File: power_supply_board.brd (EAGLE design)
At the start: 100 x 65 mm, 30 parts, among them J6 1744426-2

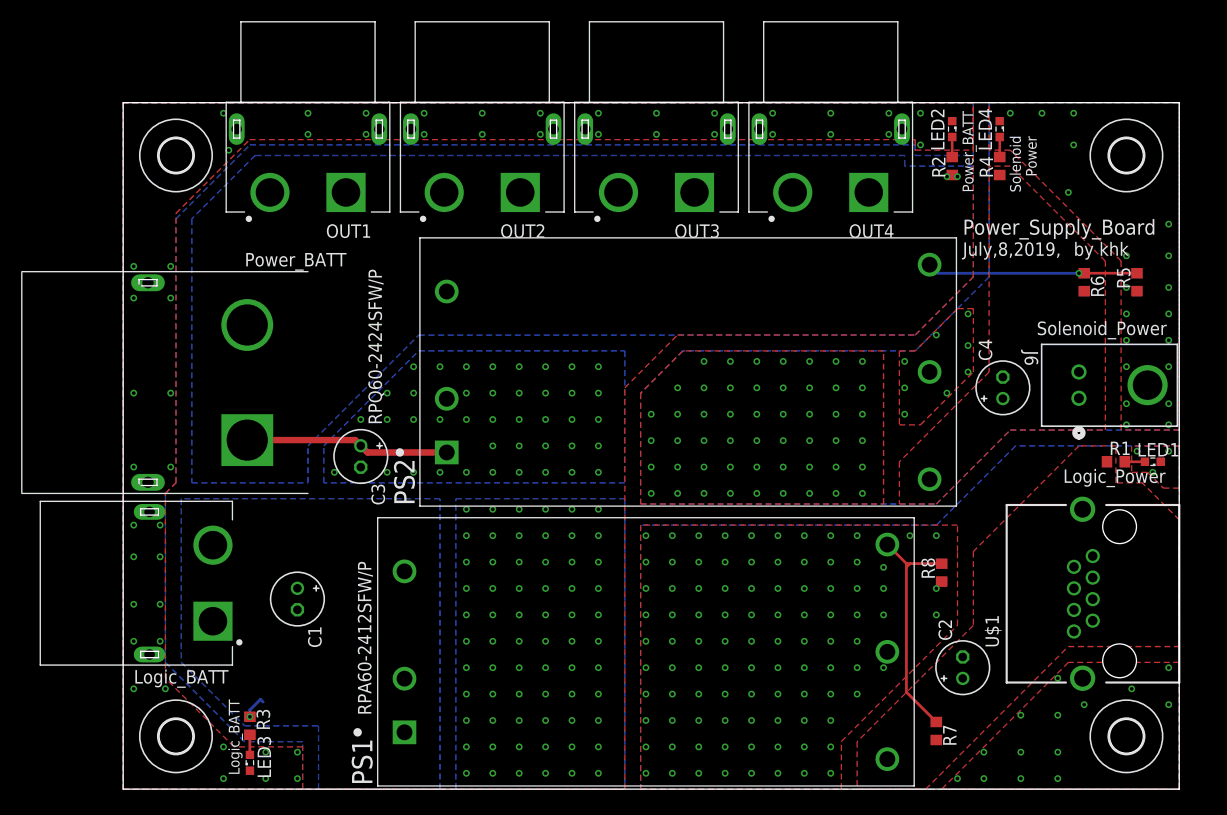
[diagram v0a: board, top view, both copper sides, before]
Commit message: xt及びコンバータのthermalを外した
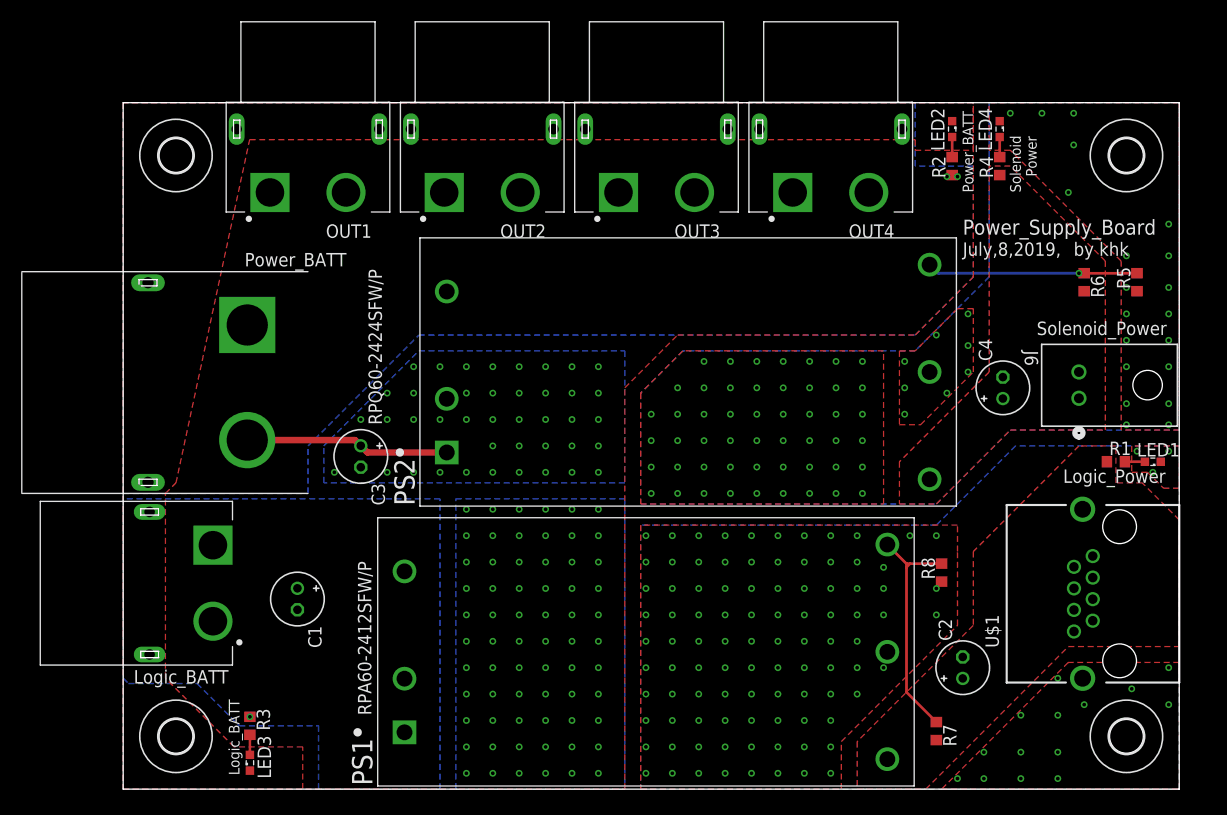
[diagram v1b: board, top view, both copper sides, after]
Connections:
- net DGND: now also OUT1.1, OUT2.1, OUT3.1, OUT4.1, POWER1.2; no longer OUT1.2, OUT2.2, OUT3.2, OUT4.2, POWER1.1
- net LOGIC_BATT: now also POWER1.1; no longer POWER1.2
- net POWER_BATT: now also OUT1.2, OUT2.2, OUT3.2, OUT4.2; no longer OUT1.1, OUT2.1, OUT3.1, OUT4.1
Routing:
- net LOGIC_BATT: track 2.42 -> 0.15 mm

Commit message: ガーバーファイルを追加
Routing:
- net POWER_BATT: track 20.5 -> 9.53 mm
- net DGND: track 0.00 -> 11.0 mm, vias 107 -> 98
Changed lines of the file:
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@@
 <setting verticaltext="up"/>
 </settings>
-<grid distance="0.5" unitdist="mm" unit="mm" style="lines" multiple="1" display="yes" altdistance="0.1" altunitdist="mm" altunit="mm"/>
+<grid distance="4" unitdist="mil" unit="mil" style="lines" multiple="1" display="yes" altdistance="2" altunitdist="mil" altunit="mil"/>
 <layers>
 <layer number="1" name="Top" color="4" fill="1" visible="yes" active="yes"/>
@@
 <text x="79.5" y="50.5" size="1.27" layer="25">July,8,2019,</text>
 <text x="90" y="50.5" size="1.27" layer="25">by khk</text>
-<rectangle x1="11.5" y1="49" x2="66" y2="54" layer="30"/>
-<rectangle x1="11.5" y1="54" x2="16.5" y2="59" layer="30"/>
-<rectangle x1="28" y1="54" x2="33" y2="59" layer="30"/>
-<rectangle x1="44.5" y1="54" x2="49.5" y2="59" layer="30"/>
-<rectangle x1="61" y1="54" x2="66" y2="59" layer="30"/>
-<rectangle x1="8.5" y1="40.5" x2="17" y2="47" layer="30"/>
-<rectangle x1="11.5" y1="47" x2="17" y2="49" layer="30"/>
+<rectangle x1="18.5" y1="49" x2="73" y2="54" layer="30"/>
+<rectangle x1="18.5" y1="54" x2="23.5" y2="59" layer="30"/>
+<rectangle x1="35" y1="54" x2="40" y2="59" layer="30"/>
+<rectangle x1="51.5" y1="54" x2="56.5" y2="59" layer="30"/>
+<rectangle x1="68" y1="54" x2="73" y2="59" layer="30"/>
+<rectangle x1="8" y1="30" x2="16.5" y2="36.5" layer="30"/>
+<rectangle x1="18.5" y1="35" x2="24" y2="49" layer="30"/>
+<rectangle x1="13" y1="32" x2="23" y2="38.5" layer="30" rot="R30"/>
 </plain>
 <attributes>
@@
 <vertex x="0" y="65"/>
 </polygon>
-<polygon width="0.254" layer="1" thermals="no">
-<vertex x="80.5" y="60.5"/>
-<vertex x="80.5" y="65"/>
-<vertex x="0" y="65"/>
-<vertex x="0" y="0"/>
-<vertex x="17" y="0"/>
-<vertex x="17" y="4"/>
-<vertex x="10.5" y="4"/>
-<vertex x="4" y="10.5"/>
-<vertex x="4" y="28"/>
-<vertex x="5" y="29"/>
-<vertex x="11.974359375" y="61.5"/>
-<vertex x="75" y="61.5"/>
-<vertex x="75" y="60.5"/>
-</polygon>
 <polygon width="0.254" layer="16">
 <vertex x="31.5" y="27.5"/>
@@
 <via x="45" y="1.5" extent="1-16" drill="0.35"/>
 <polygon width="0.254" layer="16">
-<vertex x="19" y="29"/>
-<vertex x="19" y="32.5"/>
+<vertex x="28" y="29"/>
 <vertex x="28" y="41.5"/>
 <vertex x="47.5" y="41.5"/>
@@
 <via x="32.5" y="30" extent="1-16" drill="0.35"/>
 <via x="30" y="30" extent="1-16" drill="0.35"/>
-<via x="27.5" y="30" extent="1-16" drill="0.35"/>
-<via x="25" y="30" extent="1-16" drill="0.35"/>
-<via x="20" y="30" extent="1-16" drill="0.35"/>
-<via x="25" y="35" extent="1-16" drill="0.35"/>
-<via x="22.5" y="35" extent="1-16" drill="0.35"/>
-<via x="27.5" y="35" extent="1-16" drill="0.35"/>
 <via x="30" y="35" extent="1-16" drill="0.35"/>
 <via x="32.5" y="35" extent="1-16" drill="0.35"/>
@@
 <via x="45" y="37.5" extent="1-16" drill="0.35"/>
 <via x="30" y="40" extent="1-16" drill="0.35"/>
-<via x="27.5" y="40" extent="1-16" drill="0.35"/>
-<via x="27.5" y="37.5" extent="1-16" drill="0.35"/>
-<via x="25" y="37.5" extent="1-16" drill="0.35"/>
+<wire x1="22.5" y1="30.484" x2="24.388" y2="30.484" width="0.254" layer="16"/>
+<wire x1="30.64" y1="36.736" x2="30.64" y2="36.96" width="0.254" layer="16"/>
+<wire x1="24.388" y1="30.484" x2="30.64" y2="36.736" width="0.254" layer="16"/>
 </signal>
 <signal name="POWER_BATT">
@@
 <wire x1="30.64" y1="31.88" x2="23.136" y2="31.88" width="0.6096" layer="1"/>
 <wire x1="23.136" y1="31.88" x2="22.5" y2="32.516" width="0.6096" layer="1"/>
-<wire x1="11.75" y1="33.05" x2="21.966" y2="33.05" width="0.6096" layer="1"/>
-<wire x1="21.966" y1="33.05" x2="22.5" y2="32.516" width="0.6096" layer="1"/>
 <polygon width="0.254" layer="16" thermals="no">
 <vertex x="75" y="65"/>
 <vertex x="0" y="65"/>
 <vertex x="0" y="28"/>
-<vertex x="17.5" y="28"/>
-<vertex x="17.5" y="32.5"/>
-<vertex x="28" y="43"/>
+<vertex x="27.5" y="28"/>
+<vertex x="27.5" y="42"/>
+<vertex x="28.5" y="43"/>
 <vertex x="75" y="43"/>
 <vertex x="80.5" y="48.5"/>
@@
 <contactref element="LED1" pad="A"/>
 <contactref element="R1" pad="2"/>
-<wire x1="96.75" y1="31" x2="94.85" y2="31" width="0.254" layer="1"/>
+<wire x1="96.75" y1="31" x2="94.85" y2="31" width="0.4064" layer="1"/>
 </signal>
 <signal name="N$2">
 <contactref element="LED2" pad="A"/>
 <contactref element="R2" pad="2"/>
-<wire x1="78.5" y1="61.75" x2="78.5" y2="59.85" width="0.254" layer="1"/>
+<wire x1="78.5" y1="61.75" x2="78.5" y2="59.85" width="0.4064" layer="1"/>
 </signal>
 <signal name="N$3">
 <contactref element="LED3" pad="A"/>
 <contactref element="R3" pad="2"/>
-<wire x1="12" y1="3.25" x2="12" y2="5.15" width="0.254" layer="1"/>
+<wire x1="12" y1="3.25" x2="12" y2="5.15" width="0.4064" layer="1"/>
 </signal>
 <signal name="+24V">
@@
 <contactref element="LED4" pad="A"/>
 <contactref element="R4" pad="2"/>
-<wire x1="83" y1="59.85" x2="83" y2="61.75" width="0.254" layer="1"/>
+<wire x1="83" y1="59.85" x2="83" y2="61.75" width="0.4064" layer="1"/>
 </signal>
 <signal name="GNDA">
